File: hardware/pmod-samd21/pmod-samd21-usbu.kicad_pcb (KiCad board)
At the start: 2 copper layers, 18.2 x 29 mm, 21 parts, among them J1 PMOD-2x6-MALE, J2 PMOD-2x6-FEMALE, J3 USB_C_Receptacle_USB2.0, Q1 2N7002PW, U1 ATSAMD21G-A, Y1 32.768kHz

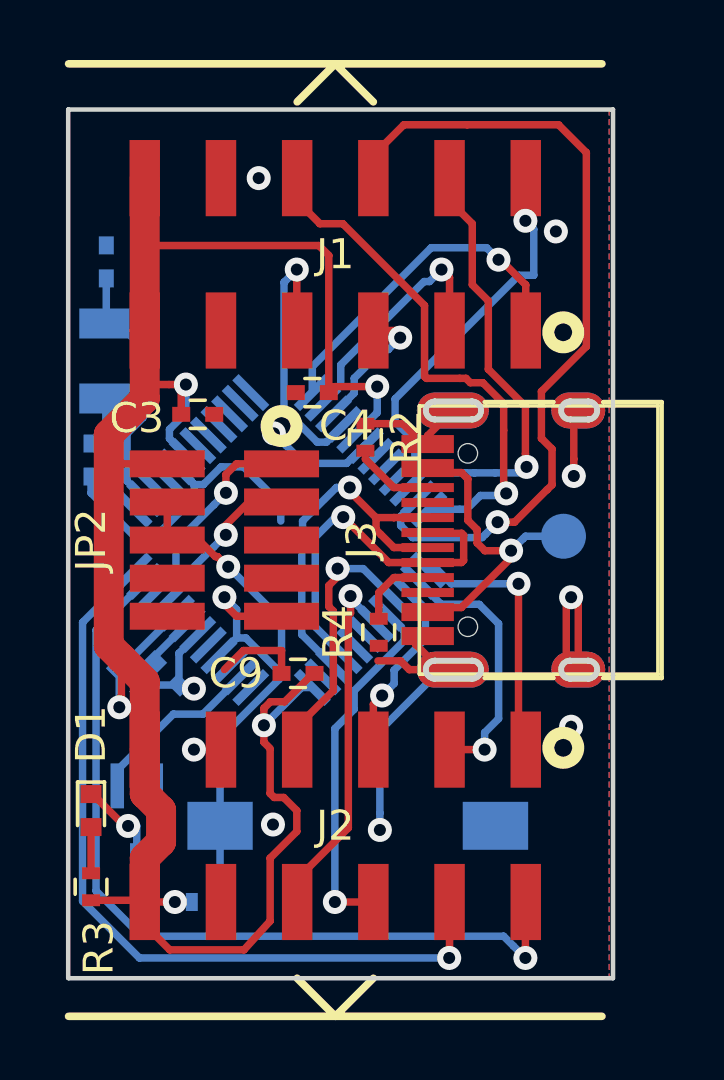
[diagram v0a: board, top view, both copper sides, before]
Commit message: SAMD21 PMOD microusb version
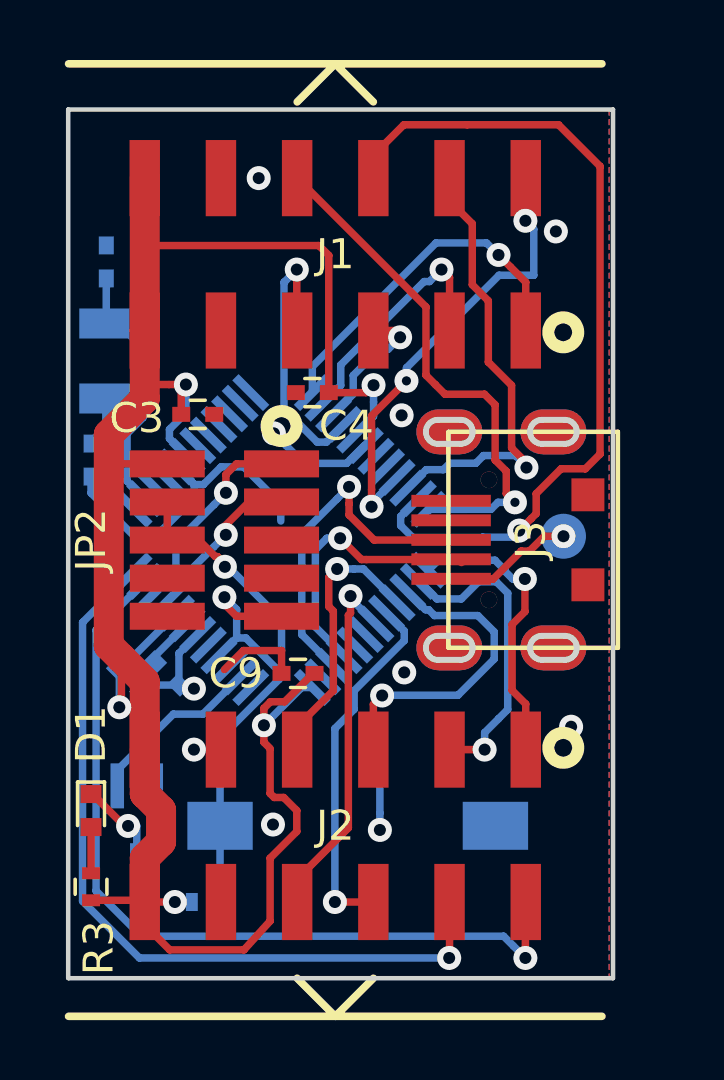
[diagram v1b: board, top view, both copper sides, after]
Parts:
- removed R2, R4: 5.1k, Resistors_SMD:R_0402
- J3: value USB_C_Receptacle_USB2.0 -> USB_B_Micro; footprint tom-connectors:USB_C_Receptacle_GT-USB-7010 -> tom-connectors:USB_MICRO_TAOBAO_SMD_PTH
- moved J3 3.19 mm to (161.1, 149.2)
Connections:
- TP1 pad 1: VBUS -> Net-(J3-Pad1)
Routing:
- net GND: track 51.2 -> 32.7 mm
- net VBUS: track 11.2 -> 0.00 mm, vias 1 -> 0
- net Net-(J3-Pad1): track 0.00 -> 4.51 mm, vias 0 -> 1
- net /SER1_2: track 6.22 -> 10.5 mm
- net /USB_D-: track 11.9 -> 8.84 mm
- net Net-(J3-PadA5): track 2.71 -> 0.00 mm
- net /SER2_0: track 12.8 -> 15.3 mm, vias 1 -> 3
- net Net-(J3-PadB5): track 2.49 -> 0.00 mm
- net /SER1_0: track 8.82 -> 10.5 mm
- net /SER1_1: track 9.58 -> 11.1 mm
- net /USB_D+: track 13.2 -> 11.8 mm
- net /SER2_2: track 27.6 -> 28.5 mm
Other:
- net class Default: clearance 0.2 -> 0.1524; trace_width 0.25 -> 0.1524; via_drill 0.4 -> 0.3048
- rule trace_clearance: 0.2 -> 0.1524
- rule trace_min: 0.2 -> 0.1524
- rule via_min_drill: 0.3 -> 0.3048
